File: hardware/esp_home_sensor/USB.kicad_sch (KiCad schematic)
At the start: 3 parts, among them J1 USB_C_Receptacle_USB2.0_16P

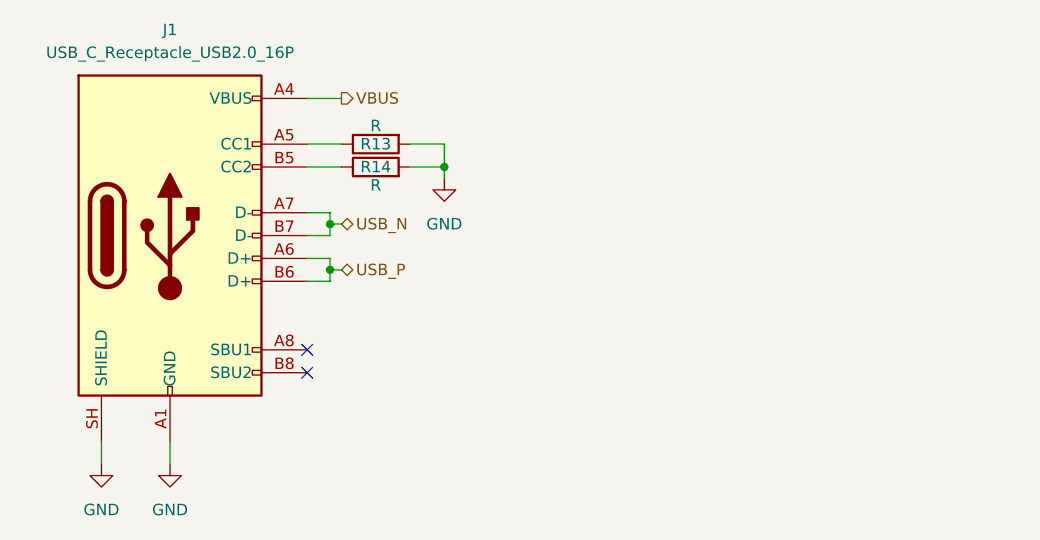
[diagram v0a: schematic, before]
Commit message: busses, display connector, footprint lib
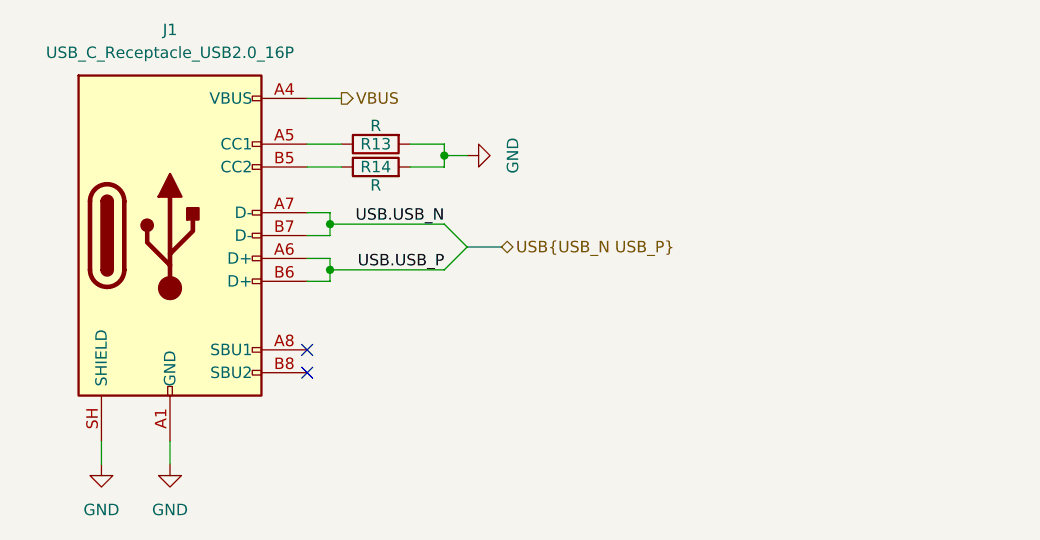
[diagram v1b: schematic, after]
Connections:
- net USB_N renamed USB.USB_N
- net USB_P renamed USB.USB_P
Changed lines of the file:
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@@
 	)
 	(junction
-		(at 132.08 92.71)
+		(at 132.08 91.44)
 		(diameter 0)
 		(color 0 0 0 0)
@@
 		(at 116.84 113.03)
 	)
+	(bus_entry
+		(at 134.62 101.6)
+		(size -2.54 2.54)
+		(stroke
+			(width 0)
+			(type default)
+		)
+	)
+	(bus_entry
+		(at 132.08 99.06)
+		(size 2.54 2.54)
+		(stroke
+			(width 0)
+			(type default)
+		)
+	)
+	(wire
+		(pts
+			(xy 134.62 91.44) (xy 132.08 91.44)
+		)
+		(stroke
+			(width 0)
+			(type default)
+		)
+	)
+	(bus
+		(pts
+			(xy 134.62 101.6) (xy 138.43 101.6)
+		)
+		(stroke
+			(width 0)
+			(type default)
+		)
+	)
 	(wire
 		(pts
@@
 	(wire
 		(pts
-			(xy 132.08 92.71) (xy 132.08 90.17)
+			(xy 132.08 92.71) (xy 132.08 91.44)
 		)
 		(stroke
@@
 	(wire
 		(pts
-			(xy 132.08 93.98) (xy 132.08 92.71)
-		)
-		(stroke
-			(width 0)
-			(type default)
-		)
-	)
-	(wire
-		(pts
 			(xy 119.38 104.14) (xy 119.38 105.41)
 		)
@@
 	(wire
 		(pts
-			(xy 119.38 99.06) (xy 120.65 99.06)
-		)
-		(stroke
-			(width 0)
-			(type default)
-		)
-	)
-	(wire
-		(pts
-			(xy 119.38 104.14) (xy 120.65 104.14)
+			(xy 119.38 99.06) (xy 132.08 99.06)
+		)
+		(stroke
+			(width 0)
+			(type default)
+		)
+	)
+	(wire
+		(pts
+			(xy 119.38 104.14) (xy 132.08 104.14)
 		)
 		(stroke
@@
 	(wire
 		(pts
+			(xy 132.08 91.44) (xy 132.08 90.17)
+		)
+		(stroke
+			(width 0)
+			(type default)
+		)
+	)
+	(wire
+		(pts
 			(xy 116.84 90.17) (xy 120.65 90.17)
 		)
@@
 			(width 0)
 			(type default)
+		)
+	)
+	(label "USB.USB_N"
+		(at 132.08 99.06 180)
+		(effects
+			(font
+				(size 1.27 1.27)
+			)
+			(justify right bottom)
+		)
+	)
+	(label "USB.USB_P"
+		(at 132.08 104.14 180)
+		(effects
+			(font
+				(size 1.27 1.27)
+			)
+			(justify right bottom)
 		)
 	)
@@
 		)
 	)
-	(hierarchical_label "USB_P"
+	(hierarchical_label "USB{USB_N USB_P}"
 		(shape bidirectional)
-		(at 120.65 104.14 0)
-		(effects
-			(font
-				(size 1.27 1.27)
-			)
-			(justify left)
-		)
-	)
-	(hierarchical_label "USB_N"
-		(shape bidirectional)
-		(at 120.65 99.06 0)
+		(at 138.43 101.6 0)
 		(effects
 			(font
@@
 	(symbol
 		(lib_id "power:GND")
-		(at 132.08 93.98 0)
-		(mirror y)
+		(at 134.62 91.44 90)
+		(mirror x)
 		(unit 1)
 		(body_style 1)
@@
 		(dnp no)
 		(property "Reference" "#PWR042"
-			(at 132.08 100.33 0)
+			(at 140.97 91.44 0)
 			(hide yes)
 			(show_name no)
@@
 		)
 		(property "Value" "GND"
-			(at 132.08 99.06 0)
+			(at 139.7 91.44 0)
 			(show_name no)
 			(do_not_autoplace no)
@@
 		)
 		(property "Footprint" ""
-			(at 132.08 93.98 0)
+			(at 134.62 91.44 0)
 			(hide yes)
 			(show_name no)
@@
 		)
 		(property "Datasheet" ""
-			(at 132.08 93.98 0)
+			(at 134.62 91.44 0)
 			(hide yes)
 			(show_name no)
@@
 		)
 		(property "Description" "Power symbol creates a global label with name \"GND\" , ground"
-			(at 132.08 93.98 0)
-			(hide yes)
-			(show_name no)
+			(at 134.62 91.44 0)
+			(hide yes)
+			(show_name no)

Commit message: footprint assignment, buck
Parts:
- J1: footprint (none) -> Connector_USB:USB_C_Receptacle_GCT_USB4110; Mfr. No. (none) -> USB4110-GF-A
- R13, R14: value R -> 5.1k; footprint (none) -> Resistor_SMD:R_0402_1005Metric
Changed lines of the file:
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@@
 			)
 		)
-		(property "Footprint" ""
+		(property "Footprint" "Connector_USB:USB_C_Receptacle_GCT_USB4110"
 			(at 105.41 100.33 0)
 			(hide yes)
@@
 		)
 		(property "Description" "USB 2.0-only 16P Type-C Receptacle connector"
+			(at 101.6 100.33 0)
+			(hide yes)
+			(show_name no)
+			(do_not_autoplace no)
+			(effects
+				(font
+					(size 1.27 1.27)
+				)
+			)
+		)
+		(property "Mfr. No." " USB4110-GF-A "
 			(at 101.6 100.33 0)
 			(hide yes)
@@
 			)
 		)
-		(property "Value" "R"
+		(property "Value" "5.1k"
 			(at 124.46 94.742 90)
 			(show_name no)
@@
 			)
 		)
-		(property "Footprint" ""
+		(property "Footprint" "Resistor_SMD:R_0402_1005Metric"
 			(at 124.46 94.488 90)
 			(hide yes)
@@
 		(property "Description" "Resistor"
 			(at 124.46 92.71 0)
+			(hide yes)
+			(show_name no)
+			(do_not_autoplace no)
+			(effects
+				(font
+					(size 1.27 1.27)
+				)
+			)
+		)
+		(property "Mfr. No." ""
+			(at 124.46 92.71 90)
 			(hide yes)
 			(show_name no)
@@
 			)
 		)
-		(property "Value" "R"
+		(property "Value" "5.1k"
 			(at 124.46 88.138 90)
 			(show_name no)
@@
 			)
 		)
-		(property "Footprint" ""
+		(property "Footprint" "Resistor_SMD:R_0402_1005Metric"
 			(at 124.46 88.392 90)
 			(hide yes)
@@
 			(hide yes)
 			(show_name no)
+			(do_not_autoplace no)
+			(effects
+				(font
+					(size 1.27 1.27)
+				)
+			)
+		)
+		(property "Mfr. No." ""
+			(at 124.46 90.17 90)
+			(hide yes)
+			(show_name no)

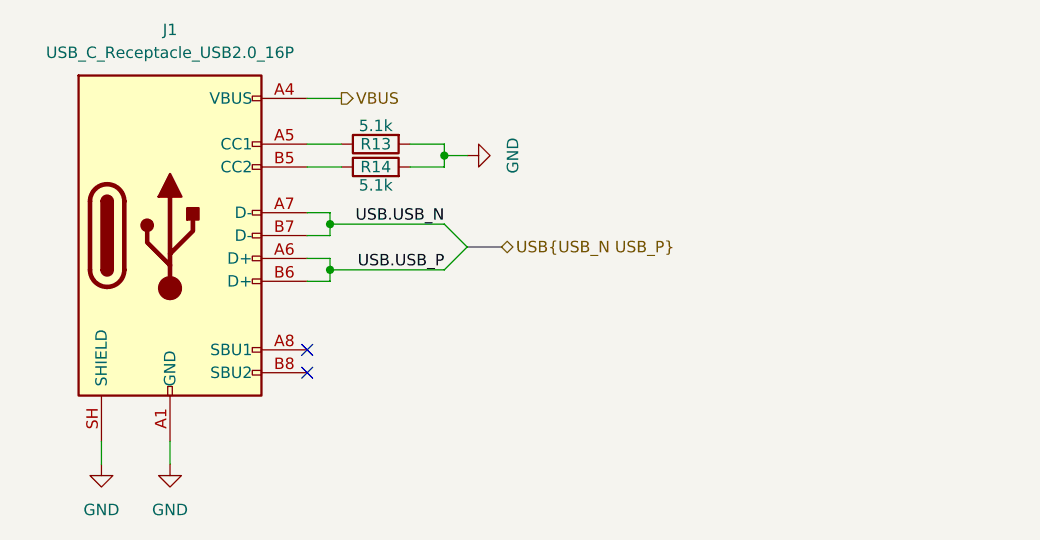
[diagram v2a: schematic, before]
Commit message: initial layout, power routing
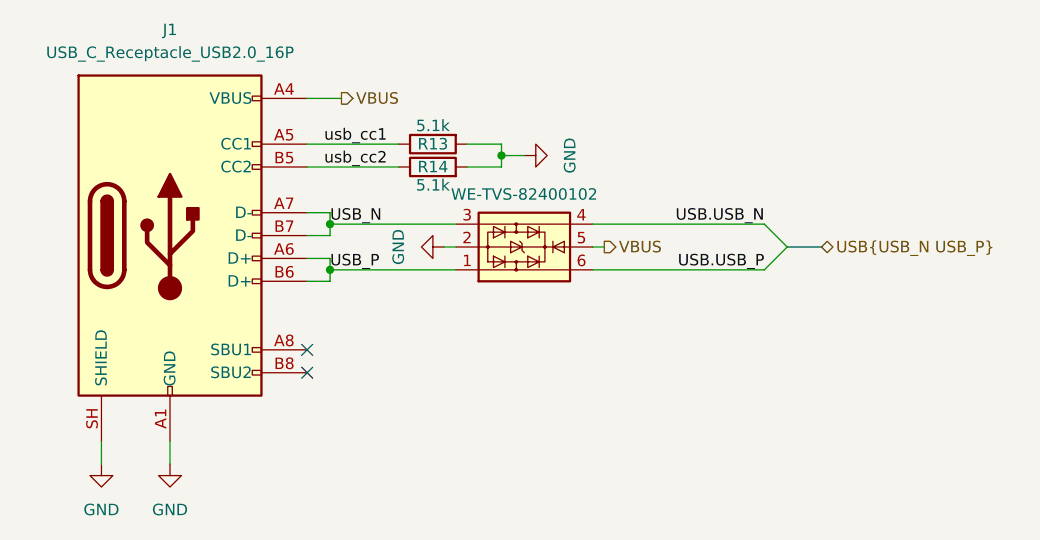
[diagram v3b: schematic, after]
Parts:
- added U4: WE-TVS-82400102, Package_TO_SOT_SMD:SOT-23-6, symbol Power_Protection:WE-TVS-82400102
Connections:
- net GND: now also U4.2
- net USB.USB_N: now also U4.4; no longer J1.A7 (D-), J1.B7 (D-)
- net USB.USB_P: now also U4.6; no longer J1.A6 (D+), J1.B6 (D+)
- net VBUS: now also U4.5
- net usb_cc1: now reaches J1.A5 (CC1), R13.1
- net usb_cc2: now reaches J1.B5 (CC2), R14.1
- new net USB_N: J1.A7 (D-), J1.B7 (D-), U4.3
- new net USB_P: J1.A6 (D+), J1.B6 (D+), U4.1
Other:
- moved on the sheet: R13, R14

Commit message: layout
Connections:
- net USB.USB_N: now also U4.6; no longer U4.4
- net USB.USB_P: now also U4.4; no longer U4.6
- net USB_N: now also U4.1; no longer U4.3
- net USB_P: now also U4.3; no longer U4.1
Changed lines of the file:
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@@
 		(lib_id "Power_Protection:WE-TVS-82400102")
 		(at 140.97 101.6 0)
-		(mirror x)
 		(unit 1)
 		(body_style 1)
@@
 		(dnp no)
 		(property "Reference" "U4"
-			(at 140.97 110.49 0)
+			(at 140.97 92.71 0)
 			(hide yes)
 			(show_name no)
@@
 		)
 		(property "Value" "WE-TVS-82400102"
-			(at 140.97 95.758 0)
+			(at 140.97 107.442 0)
 			(show_name no)
 			(do_not_autoplace no)
@@
 		)
 		(property "Footprint" "Package_TO_SOT_SMD:SOT-23-6"
-			(at 140.97 96.52 0)
+			(at 140.97 106.68 0)
 			(hide yes)
 			(show_name no)
@@
 		)
 		(property "Datasheet" "https://www.we-online.com/components/products/datasheet/82400102.pdf"
-			(at 140.97 95.25 0)
+			(at 140.97 107.95 0)
 			(hide yes)
 			(show_name no)

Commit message: layout
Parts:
- renumbered J1 to J4, R13 to R17, R14 to R18, U4 to U9
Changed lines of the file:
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@@
 		(dnp no)
 		(fields_autoplaced yes)
-		(property "Reference" "J1"
+		(property "Reference" "J4"
 			(at 101.6 77.47 0)
 			(show_name no)
@@
 			(project "esp_home_sensor"
 				(path "/1b1bee14-8d82-405b-b99d-415549a137e6/58dc3a37-e8d1-418e-8d41-d9195e52f4aa"
-					(reference "J1")
+					(reference "J4")
 					(unit 1)
 				)
@@
 		(in_pos_files yes)
 		(dnp no)
-		(property "Reference" "#PWR041"
+		(property "Reference" "#PWR055"
 			(at 101.6 132.08 0)
 			(hide yes)
@@
 			(project "esp_home_sensor"
 				(path "/1b1bee14-8d82-405b-b99d-415549a137e6/58dc3a37-e8d1-418e-8d41-d9195e52f4aa"
-					(reference "#PWR041")
+					(reference "#PWR055")
 					(unit 1)
 				)
@@
 		(in_pos_files yes)
 		(dnp no)
-		(property "Reference" "R14"
+		(property "Reference" "R18"
 			(at 130.81 92.71 90)
 			(show_name no)
@@
 			(project "esp_home_sensor"
 				(path "/1b1bee14-8d82-405b-b99d-415549a137e6/58dc3a37-e8d1-418e-8d41-d9195e52f4aa"
-					(reference "R14")
+					(reference "R18")
 					(unit 1)
 				)
@@
 		(in_pos_files yes)
 		(dnp no)
-		(property "Reference" "#PWR042"
+		(property "Reference" "#PWR057"
 			(at 147.32 91.44 0)
 			(hide yes)
@@
 			(project "esp_home_sensor"
 				(path "/1b1bee14-8d82-405b-b99d-415549a137e6/58dc3a37-e8d1-418e-8d41-d9195e52f4aa"
-					(reference "#PWR042")
+					(reference "#PWR057")
 					(unit 1)
 				)
@@
 		(in_pos_files yes)
 		(dnp no)
-		(property "Reference" "#PWR058"
+		(property "Reference" "#PWR056"
 			(at 125.73 101.6 0)
 			(hide yes)
@@
 			(project "esp_home_sensor"
 				(path "/1b1bee14-8d82-405b-b99d-415549a137e6/58dc3a37-e8d1-418e-8d41-d9195e52f4aa"
-					(reference "#PWR058")
+					(reference "#PWR056")
 					(unit 1)
 				)
@@
 		(in_pos_files yes)
 		(dnp no)
-		(property "Reference" "R13"
+		(property "Reference" "R17"
 			(at 130.81 90.17 90)
 			(show_name no)
@@
 			(project "esp_home_sensor"
 				(path "/1b1bee14-8d82-405b-b99d-415549a137e6/58dc3a37-e8d1-418e-8d41-d9195e52f4aa"
-					(reference "R13")
+					(reference "R17")
 					(unit 1)
 				)
@@
 		(in_pos_files yes)
 		(dnp no)
-		(property "Reference" "U4"
+		(property "Reference" "U9"
 			(at 140.97 92.71 0)
 			(hide yes)
@@
 			(project "esp_home_sensor"
 				(path "/1b1bee14-8d82-405b-b99d-415549a137e6/58dc3a37-e8d1-418e-8d41-d9195e52f4aa"
-					(reference "U4")
+					(reference "U9")
 					(unit 1)
 				)
@@
 		(in_pos_files yes)
 		(dnp no)
-		(property "Reference" "#PWR040"
+		(property "Reference" "#PWR054"
 			(at 93.98 132.08 0)
 			(hide yes)
@@
 			(project "esp_home_sensor"
 				(path "/1b1bee14-8d82-405b-b99d-415549a137e6/58dc3a37-e8d1-418e-8d41-d9195e52f4aa"
-					(reference "#PWR040")
-					(unit 1)
-				)
+					(reference "#PWR054")
+					(unit 1)
+				)

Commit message: in production
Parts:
- added TP30: TestPoint, TestPoint:TestPoint_Pad_D2.5mm, symbol Connector:TestPoint
- J4: Mfr. No. USB4110-GF-A -> USB4110-GF-A
- R17, R18: Mfr. No. (none) -> RC0402FR-075R1L
- U9: Mfr. No. (none) -> 82400102
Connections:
- net VBUS: now also TP30.1
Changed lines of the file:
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@@
+	)
+	(junction
+		(at 119.38 85.09)
+		(diameter 0)
+		(color 0 0 0 0)
 	)
 	(junction
@@
 	(wire
 		(pts
+			(xy 119.38 81.28) (xy 119.38 85.09)
+		)
+		(stroke
+			(width 0)
+			(type default)
+		)
+	)
+	(wire
+		(pts
 			(xy 116.84 90.17) (xy 127 90.17)
 		)
@@
 	(wire
 		(pts
+			(xy 120.65 81.28) (xy 119.38 81.28)
+		)
+		(stroke
+			(width 0)
+			(type default)
+		)
+	)
+	(wire
+		(pts
 			(xy 119.38 105.41) (xy 116.84 105.41)
 		)
@@
 	(wire
 		(pts
+			(xy 119.38 85.09) (xy 120.65 85.09)
+		)
+		(stroke
+			(width 0)
+			(type default)
+		)
+	)
+	(wire
+		(pts
 			(xy 119.38 102.87) (xy 119.38 104.14)
 		)
@@
 	(wire
 		(pts
-			(xy 116.84 85.09) (xy 120.65 85.09)
+			(xy 116.84 85.09) (xy 119.38 85.09)
 		)
 		(stroke
@@
 			)
 		)
-		(property "Mfr. No." " USB4110-GF-A "
+		(property "Mfr. No." " USB4110-GF-A"
 			(at 101.6 100.33 0)
 			(hide yes)
@@
 				(path "/1b1bee14-8d82-405b-b99d-415549a137e6/58dc3a37-e8d1-418e-8d41-d9195e52f4aa"
 					(reference "J4")
+					(unit 1)
+				)
+			)
+		)
+	)
+	(symbol
+		(lib_id "Connector:TestPoint")
+		(at 120.65 81.28 270)
+		(unit 1)
+		(body_style 1)
+		(exclude_from_sim no)
+		(in_bom no)
+		(on_board yes)
+		(in_pos_files yes)
+		(dnp no)
+		(property "Reference" "TP30"
+			(at 125.73 81.28 90)
+			(show_name no)
+			(do_not_autoplace no)
+			(effects
+				(font
+					(size 1.27 1.27)
+				)
+				(justify left)
+			)
+		)
+		(property "Value" "TestPoint"
+			(at 125.73 82.5499 90)
+			(hide yes)
+			(show_name no)
+			(do_not_autoplace no)
+			(effects
+				(font
+					(size 1.27 1.27)
+				)
+				(justify left)
+			)
+		)
+		(property "Footprint" "TestPoint:TestPoint_Pad_D2.5mm"
+			(at 120.65 86.36 0)
+			(hide yes)
+			(show_name no)
+			(do_not_autoplace no)
+			(effects
+				(font
+					(size 1.27 1.27)
+				)
+			)
+		)
+		(property "Datasheet" ""
+			(at 120.65 86.36 0)
+			(hide yes)
+			(show_name no)
+			(do_not_autoplace no)
+			(effects
+				(font
+					(size 1.27 1.27)
+				)
+			)
+		)
+		(property "Description" "test point"
+			(at 120.65 81.28 0)
+			(hide yes)
+			(show_name no)
+			(do_not_autoplace no)
+			(effects
+				(font
+					(size 1.27 1.27)
+				)
+			)
+		)
+		(pin "1"
+		)
+		(instances
+			(project "esp_home_sensor"
+				(path "/1b1bee14-8d82-405b-b99d-415549a137e6/58dc3a37-e8d1-418e-8d41-d9195e52f4aa"
+					(reference "TP30")
 					(unit 1)
 				)
@@
 			)
 		)
-		(property "Mfr. No." ""
+		(property "Mfr. No." "RC0402FR-075R1L"
 			(at 130.81 92.71 90)
 			(hide yes)
@@
 			)
 		)
-		(property "Mfr. No." ""
+		(property "Mfr. No." "RC0402FR-075R1L"
 			(at 130.81 90.17 90)
 			(hide yes)
@@
 			(at 140.97 101.6 0)
 			(hide yes)
+			(show_name no)
+			(do_not_autoplace no)
+			(effects
+				(font
+					(size 1.27 1.27)
+				)
+			)
+		)
+		(property "Mfr. No." "82400102"
+			(at 140.97 101.6 0)
+			(hide yes)

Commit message: az
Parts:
- U9: Down_current (none) -> 1u; Supply_current (none) -> 1u
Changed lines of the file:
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@@
+			)
+		)
+		(property "Down_current" ""
+			(at 101.6 100.33 0)
+			(hide yes)
+			(show_name no)
+			(do_not_autoplace no)
+			(effects
+				(font
+					(size 1.27 1.27)
+				)
+			)
+		)
+		(property "Supply_current" ""
+			(at 101.6 100.33 0)
+			(hide yes)
+			(show_name no)
+			(do_not_autoplace no)
+			(effects
+				(font
+					(size 1.27 1.27)
+				)
 			)
 		)
@@
 		(property "Description" "test point"
 			(at 120.65 81.28 0)
+			(hide yes)
+			(show_name no)
+			(do_not_autoplace no)
+			(effects
+				(font
+					(size 1.27 1.27)
+				)
+			)
+		)
+		(property "Down_current" ""
+			(at 120.65 81.28 90)
+			(hide yes)
+			(show_name no)
+			(do_not_autoplace no)
+			(effects
+				(font
+					(size 1.27 1.27)
+				)
+			)
+		)
+		(property "Supply_current" ""
+			(at 120.65 81.28 90)
 			(hide yes)
 			(show_name no)
@@
 			)
 		)
+		(property "Down_current" ""
+			(at 130.81 92.71 90)
+			(hide yes)
+			(show_name no)
+			(do_not_autoplace no)
+			(effects
+				(font
+					(size 1.27 1.27)
+				)
+			)
+		)
+		(property "Supply_current" ""
+			(at 130.81 92.71 90)
+			(hide yes)
+			(show_name no)
+			(do_not_autoplace no)
+			(effects
+				(font
+					(size 1.27 1.27)
+				)
+			)
+		)
 		(pin "1"
 		)
@@
 			)
 		)
+		(property "Down_current" ""
+			(at 130.81 90.17 90)
+			(hide yes)
+			(show_name no)
+			(do_not_autoplace no)
+			(effects
+				(font
+					(size 1.27 1.27)
+				)
+			)
+		)
+		(property "Supply_current" ""
+			(at 130.81 90.17 90)
+			(hide yes)
+			(show_name no)
+			(do_not_autoplace no)
+			(effects
+				(font
+					(size 1.27 1.27)
+				)
+			)
+		)
 		(pin "1"
 		)
@@
 			(at 140.97 101.6 0)
 			(hide yes)
+			(show_name no)
+			(do_not_autoplace no)
+			(effects
+				(font
+					(size 1.27 1.27)
+				)
+			)
+		)
+		(property "Down_current" "1u"
+			(at 140.97 101.6 0)
+			(hide yes)
+			(show_name no)
+			(do_not_autoplace no)
+			(effects
+				(font
+					(size 1.27 1.27)
+				)
+			)
+		)
+		(property "Supply_current" "1u"
+			(at 140.97 101.6 0)
+			(hide yes)
